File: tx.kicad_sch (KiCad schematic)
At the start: 28 parts, among them Q301 MMBF170, Q302 MMBF170, Q303 MMBF170, Q304 MMBF170, Q305 MMBF170, Q306 MMBF170, Q307 MMBF170, Q308 MMBF170, Q309 MMBF170, Q310 MMBF170, Q311 MMBF170, Q312 MMBF170, T301 BN-43-202_DualPri_CTSec, U301 CD74AC244M

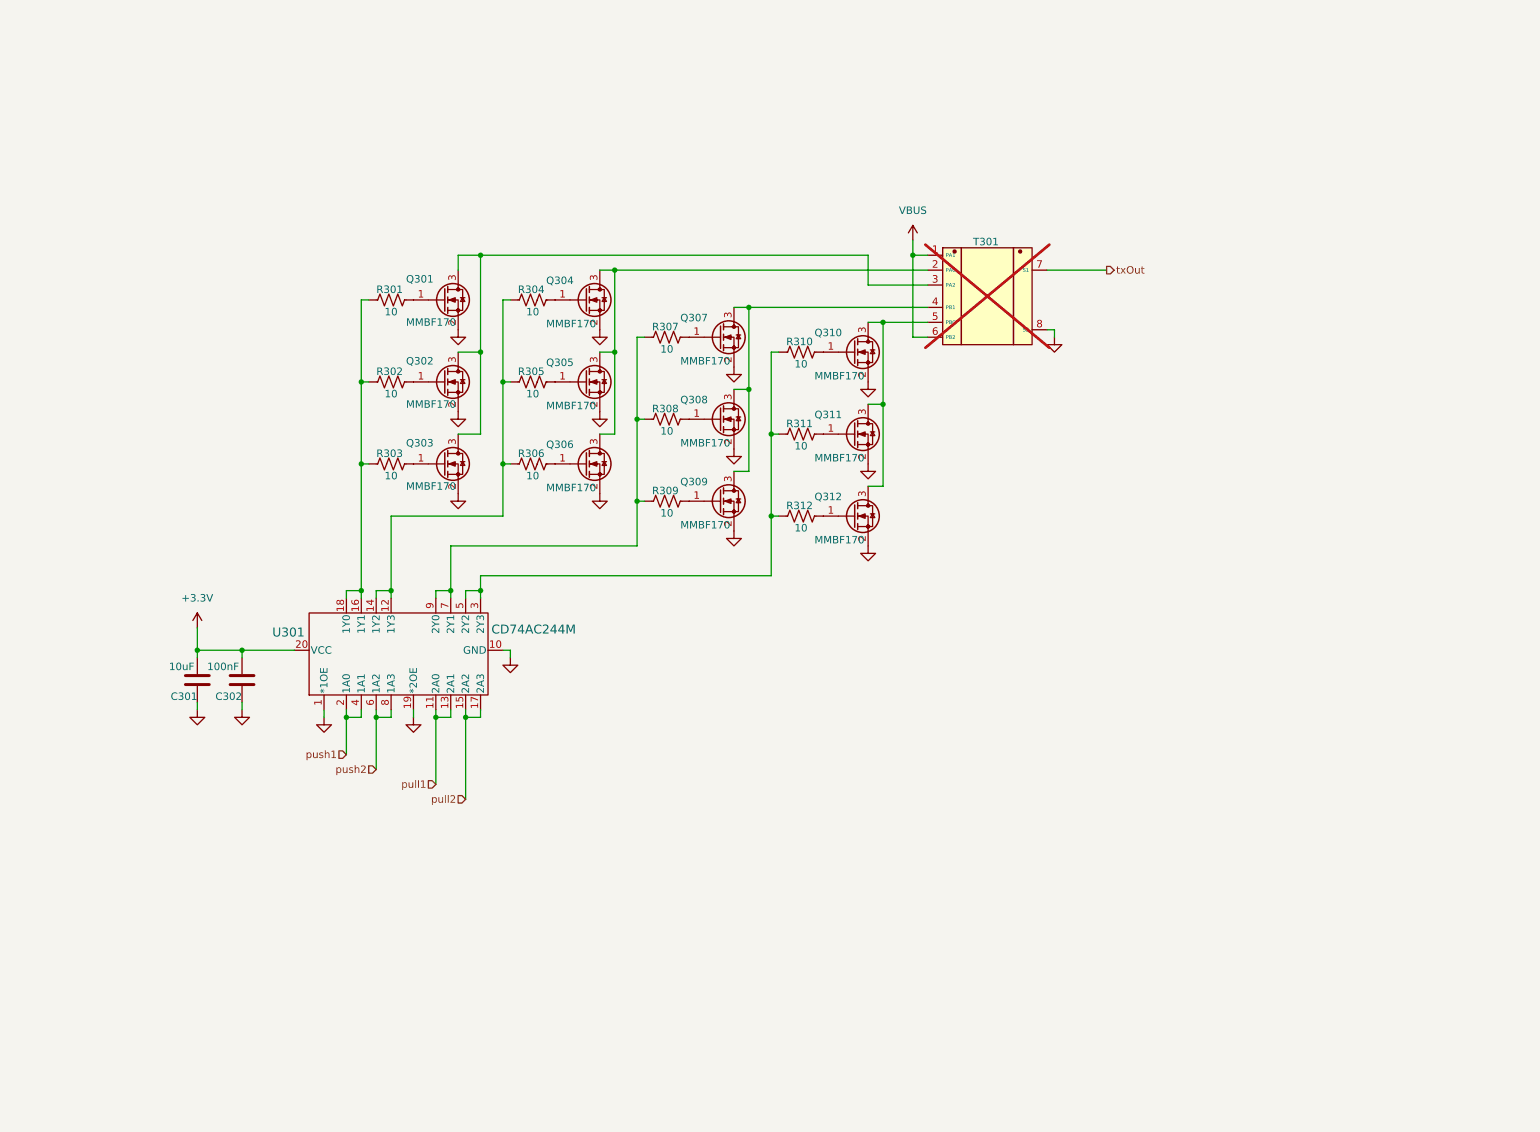
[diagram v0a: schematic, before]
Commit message: Fix filters for proper response. Now we have FPGA + ESP32S3.
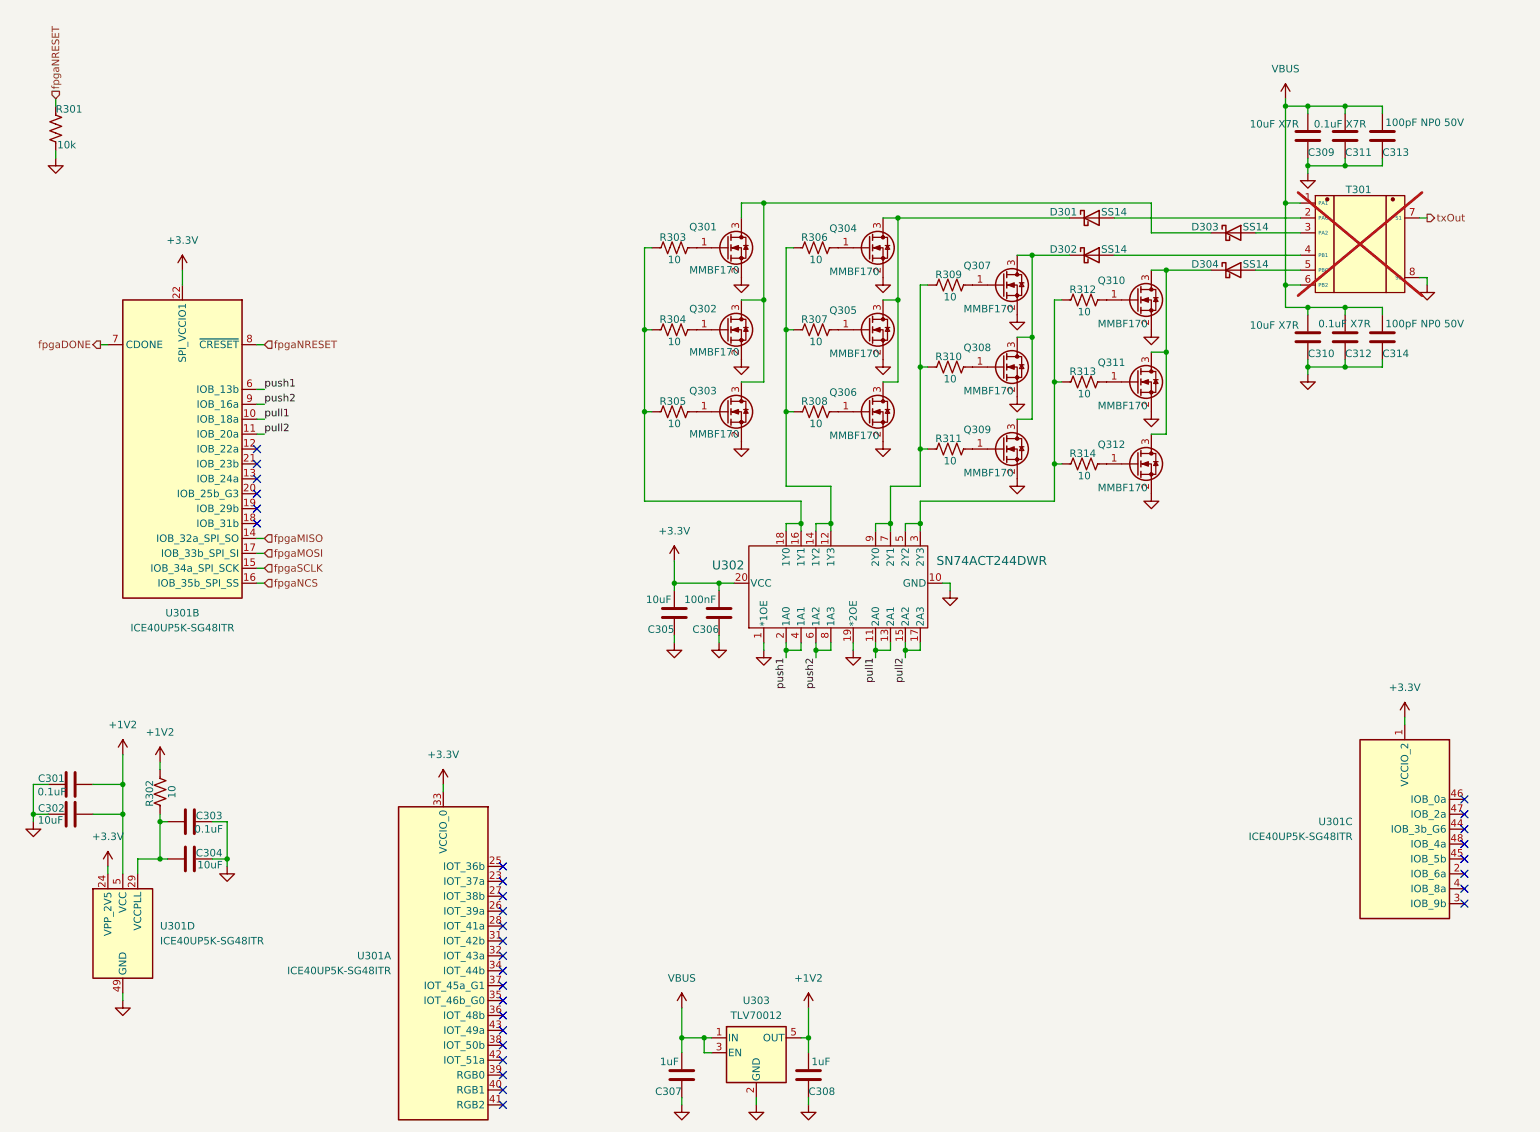
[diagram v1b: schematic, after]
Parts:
- added C301, C303: 0.1uF, Capacitor_SMD:C_0603_1608Metric, symbol Device:C
- added C302, C304: 10uF, Capacitor_SMD:C_0603_1608Metric, symbol Device:C
- added C307, C308: 1uF, Capacitor_SMD:C_0603_1608Metric, symbol Device:C
- added C309, C310: 10uF X7R, Capacitor_SMD:C_0603_1608Metric, symbol Device:C
- added C311, C312: 0.1uF X7R, Capacitor_SMD:C_0603_1608Metric, symbol Device:C
- added C313, C314: 100pF NP0 50V, Capacitor_SMD:C_0603_1608Metric, symbol Device:C
- added D301, D302, D303, D304: SS14, Diode_SMD:D_SMA, symbol Diode:SS14
- added R301: 10k, symbol Device:R_US
- added R302: 10, Resistor_SMD:R_0603_1608Metric, symbol Device:R_US
- added U301: ICE40UP5K-SG48ITR, Package_DFN_QFN:QFN-48-1EP_7x7mm_P0.5mm_EP5.6x5.6mm, symbol FPGA_Lattice:ICE40UP5K-SG48ITR
- added U303: TLV70012, Package_TO_SOT_SMD:SOT-353_SC-70-5, symbol Regulator_Linear:TLV70012_SOT353
- U302: renamed from U301; value CD74AC244M -> SN74ACT244DWR; MFG (none) -> Texas Instruments; MPN (none) -> SN74ACT244DWR
- renumbered C301 to C305, C302 to C306, R301 to R303, R302 to R304, R303 to R305, R304 to R306, R305 to R307, R306 to R308, R307 to R309, R308 to R310, R309 to R311, R310 to R312, R311 to R313, R312 to R314
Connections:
- net +3.3V: now also U301.1 (VCCIO_2), U301.22 (SPI_VCCIO1), U301.24 (VPP_2V5), U301.33 (VCCIO_0)
- net GND: now also C301.1, C302.1, C303.1, C304.1, C307.1, C308.1, C309.1, C310.1, C311.1, C312.1, C313.1, C314.1, R301.2, U301.49 (GND), U303.2 (GND)
- net VBUS: now also C307.2, C309.2, C310.2, C311.2, C312.2, C313.2, C314.2, U303.1 (IN), U303.3 (EN)
- net pull1: now also U301.10 (IOB_18a)
- net pull2: now also U301.11 (IOB_20a)
- net push1: now also U301.6 (IOB_13b)
- net push2: now also U301.9 (IOB_16a)
- net at Q301.3 (D), Q302.3 (D), Q303.3 (D): now also D303.1 (K); no longer T301.3 (PA2)
- net at Q307.3 (D), Q308.3 (D), Q309.3 (D): now also D302.1 (K); no longer T301.4 (PB1)
- net at Q310.3 (D), Q311.3 (D), Q312.3 (D): now also D304.1 (K); no longer T301.5 (PBC)
- net at Q304.3 (D), Q305.3 (D), Q306.3 (D): now also D301.1 (K); no longer T301.2 (PAC)
- new net: D303.2 (A), T301.3 (PA2)
- new net: C303.2, C304.2, R302.1, U301.29 (VCCPLL)
- new net: D304.2 (A), T301.5 (PBC)
- new net: D301.2 (A), T301.2 (PAC)
- new net: D302.2 (A), T301.4 (PB1)
- new net +1V2: C301.2, C302.2, C308.2, R302.2, U301.30 (VCC), U301.5 (VCC), U303.5 (OUT)
- new net fpgaDONE: U301.7 (CDONE)
- new net fpgaMISO: U301.14 (IOB_32a_SPI_SO)
- new net fpgaMOSI: U301.17 (IOB_33b_SPI_SI)
- new net fpgaNCS: U301.16 (IOB_35b_SPI_SS)
- new net fpgaNRESET: R301.1, U301.8 (~{CRESET})
- new net fpgaSCLK: U301.15 (IOB_34a_SPI_SCK)
- no-connect marks 0 -> 31
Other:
- moved on the sheet: C305, C306, Q301, Q302, Q303, Q304, Q305, Q306, Q307, Q308, Q309, Q310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

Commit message: Well it is routed and passes DRC
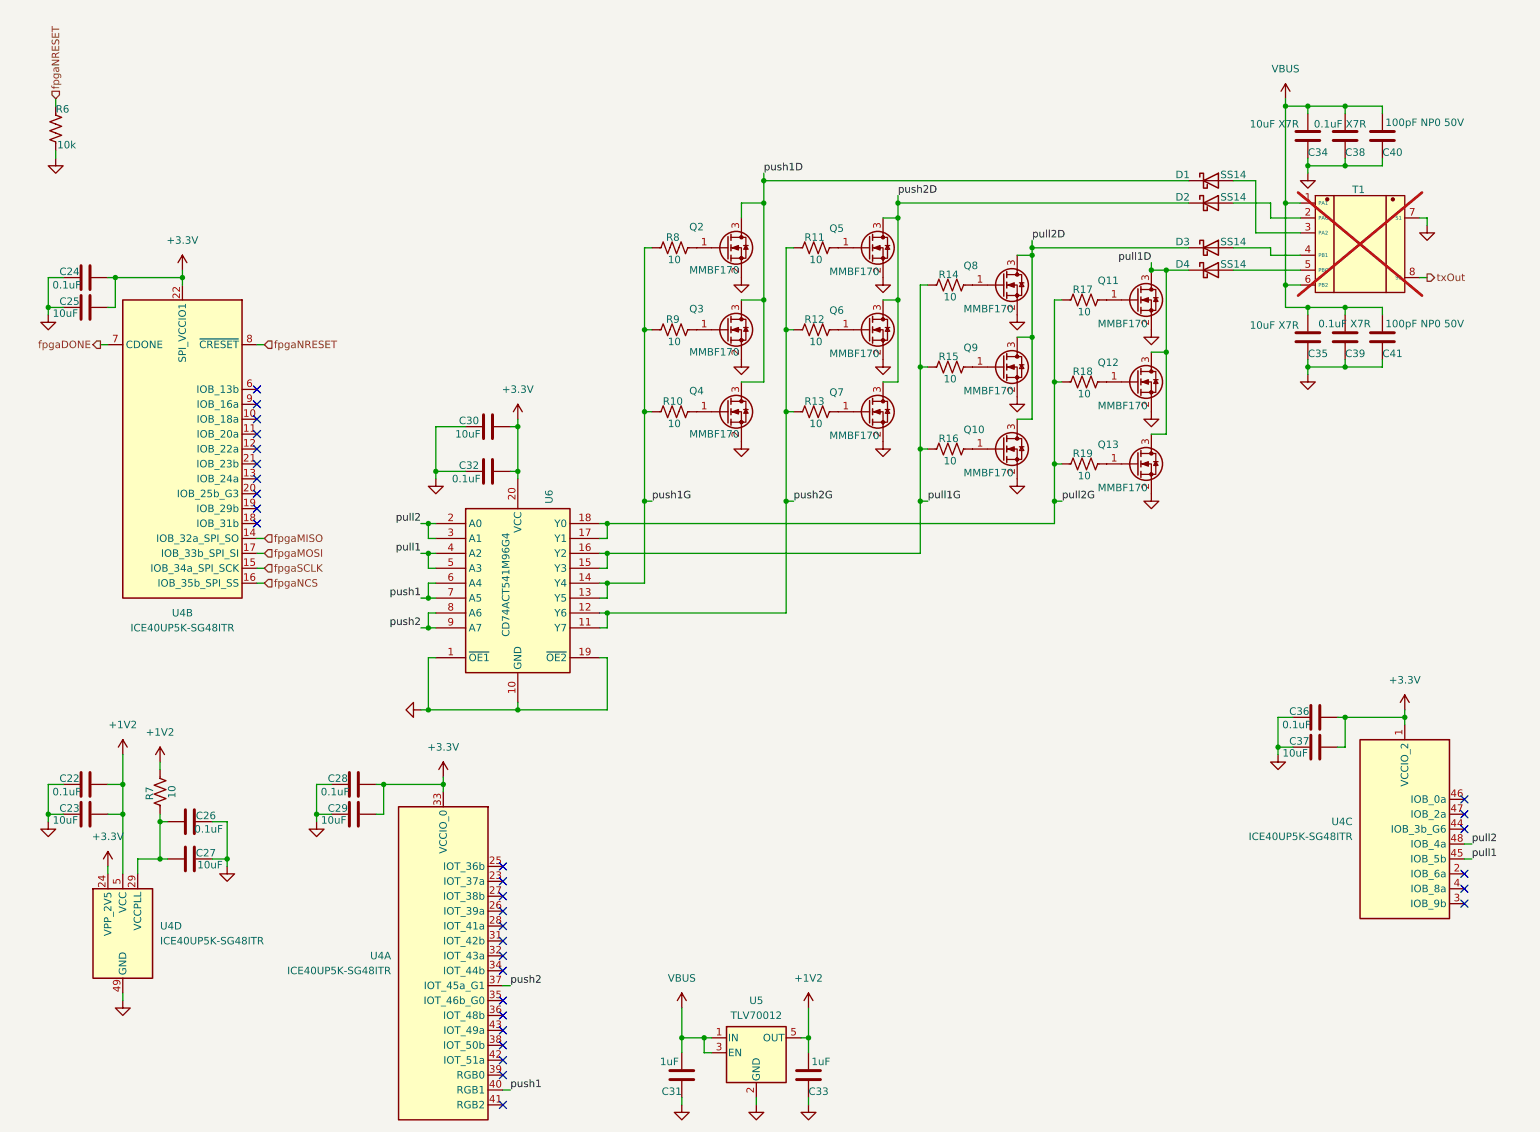
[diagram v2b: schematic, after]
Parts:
- removed D301, D302, D304: SS14, Diode_SMD:D_SMA, symbol Diode:SS14
- removed U302: SN74ACT244DWR, DW20, symbol Library:CD74AC244M
- added C24, C28, C36: 0.1uF, Capacitor_SMD:C_0603_1608Metric, symbol Device:C
- added C25, C29, C37: 10uF, Capacitor_SMD:C_0603_1608Metric, symbol Device:C
- added D2, D3, D4: SS14, Diode_SMD:D_SMA, symbol Diode:SS14
- added U6: CD74ACT541M96G4, SOIC127P1030X265-20N, symbol Library:CD74ACT541M96G4
- C32: renamed from C306; value 100nF -> 0.1uF
- R6: renamed from R301; footprint (none) -> Resistor_SMD:R_0603_1608Metric
- renumbered C301 to C22, C302 to C23, C303 to C26, C304 to C27, C305 to C30, C307 to C31, C308 to C33, C309 to C34, C310 to C35, C311 to C38, C312 to C39, C313 to C40, C314 to C41, D303 to D1, Q309 to Q10, Q310 to Q11, Q311 to Q12, Q312 to Q13, Q301 to Q2, Q302 to Q3, Q303 to Q4, Q304 to Q5, Q305 to Q6, Q306 to Q7, Q307 to Q8, Q308 to Q9, R305 to R10, R306 to R11, R307 to R12, R308 to R13, R309 to R14, R310 to R15, R311 to R16, R312 to R17, R313 to R18, R314 to R19, R302 to R7, R303 to R8, R304 to R9, T301 to T1, U301 to U4, U303 to U5
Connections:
- net +3.3V: now also C24.2, C25.2, C28.2, C29.2, C36.2, C37.2, U6.20 (VCC)
- net GND: now also T1.7 (S1), C24.1, C25.1, C28.1, C29.1, C36.1, C37.1, U6.1 (~{OE1}), U6.10 (GND), U6.19 (~{OE2}); no longer T1.8 (S2)
- net pull1: now also U4.45 (IOB_5b), U6.4 (A2), U6.5 (A3); no longer U4.10 (IOB_18a)
- net pull2: now also U4.48 (IOB_4a), U6.2 (A0), U6.3 (A1); no longer U4.11 (IOB_20a)
- net push1: now also U4.40 (RGB1), U6.6 (A4), U6.7 (A5); no longer U4.6 (IOB_13b)
- net push2: now also U4.37 (IOT_45a_G1), U6.8 (A6), U6.9 (A7); no longer U4.9 (IOB_16a)
- net txOut: now also T1.8 (S2); no longer T1.7 (S1)
- net push1D: now reaches D1.1 (K), Q2.3 (D), Q3.3 (D), Q4.3 (D)
- net push2G: now reaches R11.1, R12.1, R13.1
- net push2G: now also U6.11 (Y7), U6.12 (Y6)
- net push1G: now reaches R10.1, R8.1, R9.1
- net push1G: now also U6.13 (Y5), U6.14 (Y4)
- net pull2D: now reaches Q10.3 (D), Q8.3 (D), Q9.3 (D)
- net pull2D: now also D3.1 (K)
- net pull1D: now reaches Q11.3 (D), Q12.3 (D), Q13.3 (D)
- net pull1D: now also D4.1 (K)
- net at T1.5 (PBC): now also D4.2 (A)
- net pull2G: now reaches R17.1, R18.1, R19.1
- net pull2G: now also U6.17 (Y1), U6.18 (Y0)
- net push2D: now reaches Q5.3 (D), Q6.3 (D), Q7.3 (D)
- net push2D: now also D2.1 (K)
- net at T1.2 (PAC): now also D2.2 (A)
- net at T1.4 (PB1): now also D3.2 (A)
- net pull1G: now reaches R14.1, R15.1, R16.1
- net pull1G: now also U6.15 (Y3), U6.16 (Y2)
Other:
- moved on the sheet: C22, C23, C30, C32, D1

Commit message: Minor tweaks after submitting 001 build to pcbway
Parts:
- added R20, R21, R22, R23: 10k, Resistor_SMD:R_0603_1608Metric, symbol Device:R_US
- Q10, Q11, Q12, Q13, Q2, Q3, Q4, Q5, Q6, Q7, Q8, Q9: LCSC (none) -> C28871
- T1: now fitted; now left out of the parts list
- U4: LCSC (none) -> C2678152
- U5: LCSC (none) -> C69446
- U6: LCSC (none) -> C899000; MPN (none) -> 74ACT541SCX; Manufacturer_Name Texas Instruments -> onsemi; Mouser Part Number 595-CD74ACT541M96G4 -> 74ACT541SCX; Mouser Price/Stock https://www.mouser.co.uk/ProductDetail/Texas-Instruments/CD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 -> https://www.lcsc.com/datasheet/C899000.pdf
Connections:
- net GND: now also R20.2, R21.2, R22.2, R23.2
- net pull1: now also R20.1
- net pull1D: now also D3.1 (K), Q10.3 (D), Q8.3 (D), Q9.3 (D); no longer D4.1 (K), Q11.3 (D), Q12.3 (D), Q13.3 (D)
- net pull2: now also R21.1
- net pull2D: now also D4.1 (K), Q11.3 (D), Q12.3 (D), Q13.3 (D); no longer D3.1 (K), Q10.3 (D), Q8.3 (D), Q9.3 (D)
- net push1: now also U4.42 (IOT_51a), R22.1; no longer U4.40 (RGB1)
- net push2: now also R23.1
- net push1T: now reaches D1.2 (A), T1.3 (PA2)
- net pull1T: now reaches D3.2 (A), T1.4 (PB1)
- net push2T: now reaches D2.2 (A), T1.2 (PAC)
- net pull2T: now reaches D4.2 (A), T1.5 (PBC)
